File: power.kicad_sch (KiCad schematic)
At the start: 71 parts, among them J7 USB-C_GCT_USB4105-GF-A, J8 Molex_Nano-Fit_1x2_SMD_105430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, Q3 2N7002_SOT-23-3, U13 TPS564247DRLR, U6 TPS564247DRLR, U7 TPS564247DRLR, U8 TPS564247DRLR, U9 TPS564247DRLR

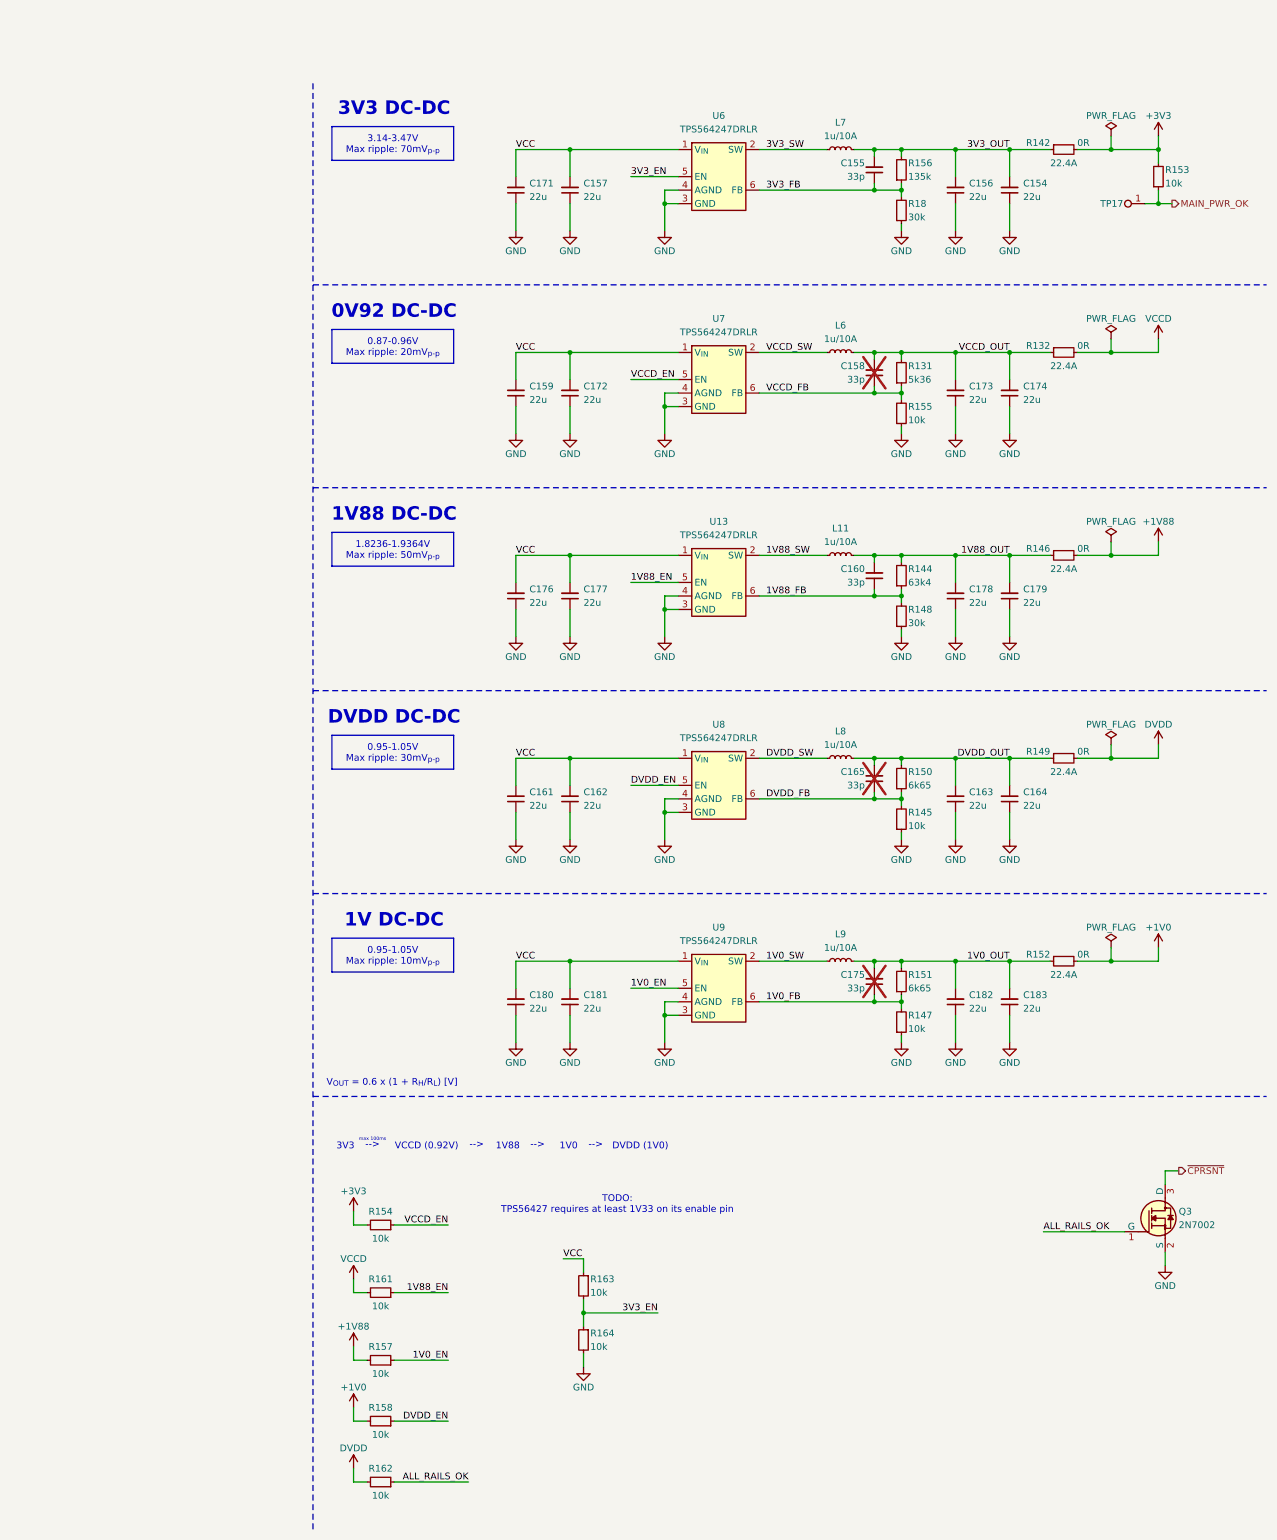
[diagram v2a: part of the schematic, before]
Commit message: [#85196] Draft DC-DC converters with new IC
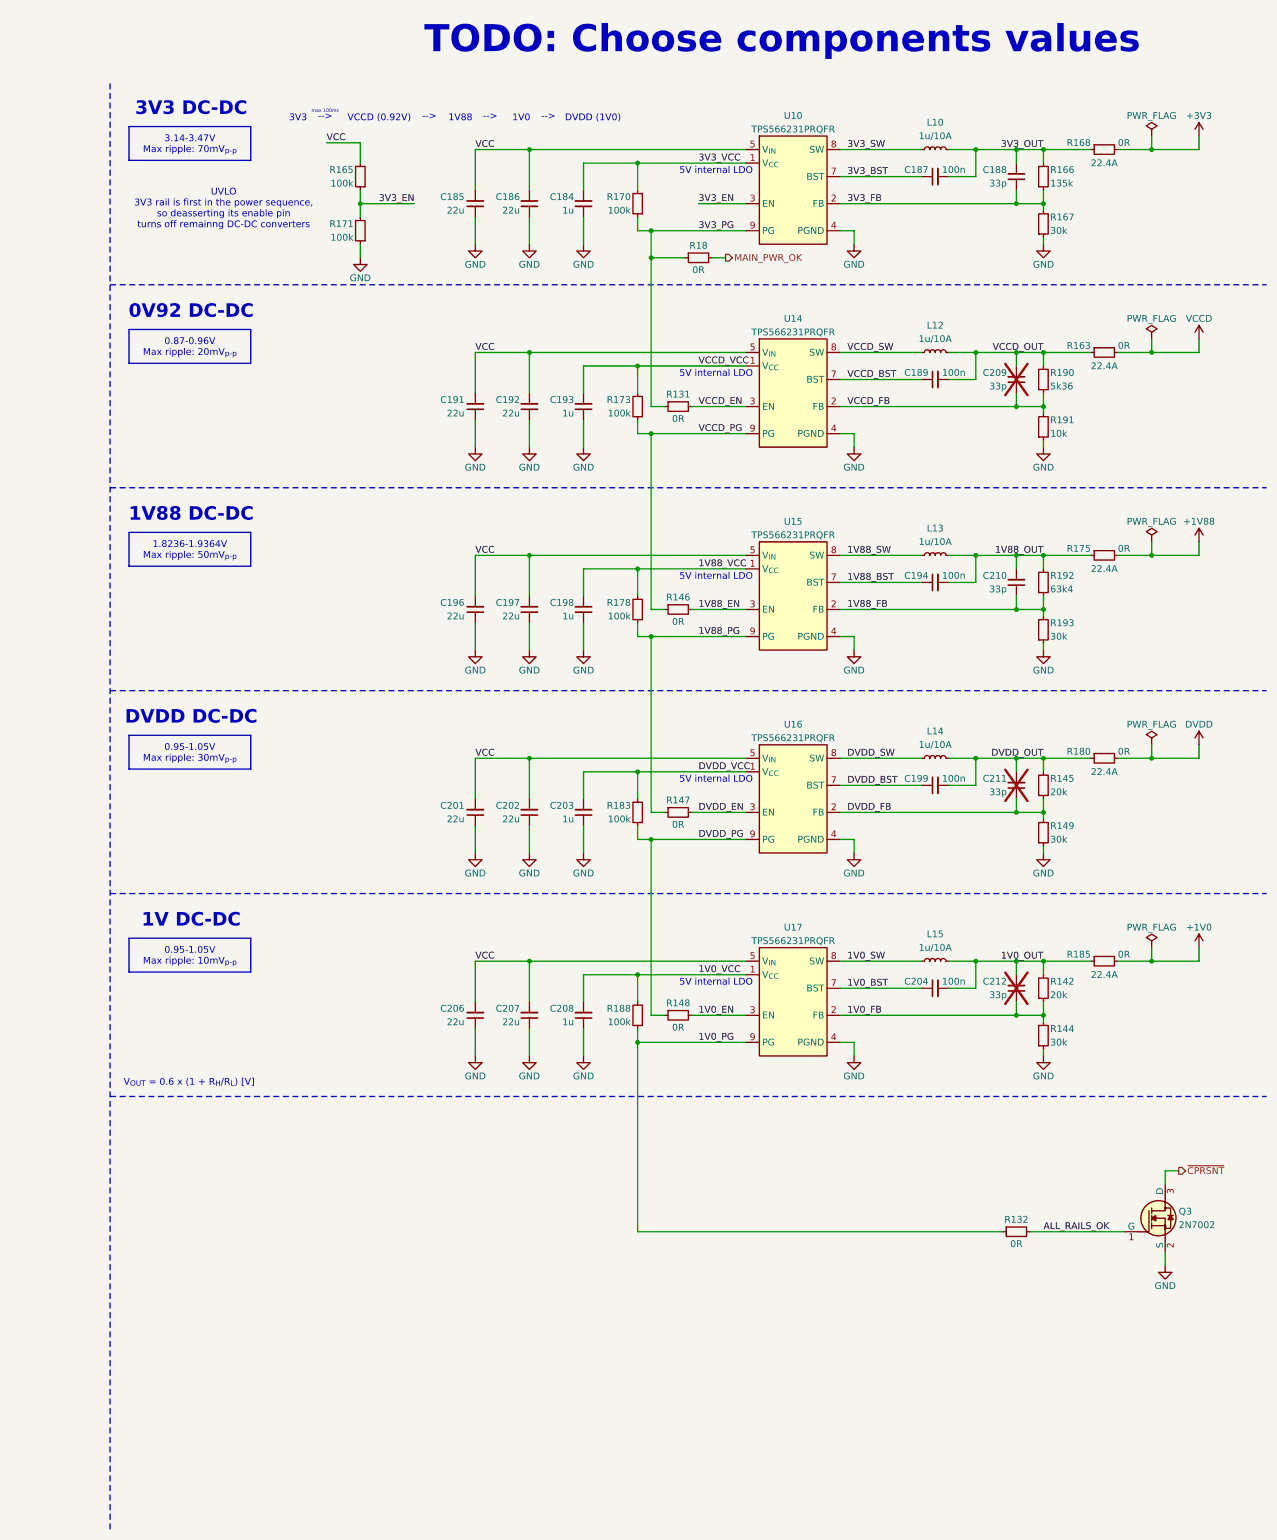
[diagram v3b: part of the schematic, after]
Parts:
- removed C154, C156, C157, C159, C161, C162, C163, C164, C171, C172, C173, C174, C176, C177, C178, C179, C180, C181, C182, C183: C_22u_16V_0603, antmicro-footprints:C_0603_1608Metric_EIA, symbol antmicroCapacitors0603:C_22u_16V_0603
- removed C155, C158, C160, C165, C175: C_33p_0402, antmicro-footprints:C_0402_1005Metric, symbol antmicroCapacitors0402:C_33p_0402
- removed L11, L6, L7, L8, L9: L_1u_10A_Bourns-SRP4021HMT, antmicro-footprints:L_Bourns-SRP4021HMT, symbol antmicroFixedInductors:L_1u_10A_Bourns-SRP4021HMT
- removed R131: R_5k36_0402, antmicro-footprints:R_0402_1005Metric, symbol antmicroResistors0402:R_5k36_0402
- removed R132, R142, R146, R149, R152: R_0R_22.4A_0603, antmicro-footprints:R_0603_1608Metric, symbol antmicroResistors0603:R_0R_22.4A_0603
- removed R144: R_63k4_0402, antmicro-footprints:R_0402_1005Metric, symbol antmicroResistors0402:R_63k4_0402
- removed R145, R147, R155: R_10k_0.1%_0402, antmicro-footprints:R_0402_1005Metric, symbol antmicroResistors0402:R_10k_0.1%_0402
- removed R148, R18: R_30k_0402, antmicro-footprints:R_0402_1005Metric, symbol antmicroResistors0402:R_30k_0402
- removed R150, R151: R_6k65_0402, antmicro-footprints:R_0402_1005Metric, symbol antmicroResistors0402:R_6k65_0402
- removed R153, R154, R157, R158, R161, R162, R163, R164: R_10k_0402, antmicro-footprints:R_0402_1005Metric, symbol antmicroResistors0402:R_10k_0402
- removed R156: R_135k_0402, antmicro-footprints:R_0402_1005Metric, symbol antmicroResistors0402:R_135k_0402
- removed TP17: TP_0.75mm_SMD, antmicro-footprints:TP_SMD_0.75mm, symbol antmicroTestPoints:TP_0.75mm_SMD
- removed U13, U6, U7, U8, U9: TPS564247DRLR, antmicro-footprints:SOT-563, symbol antmicroDCDCConverters:TPS564247DRLR
- added C184, C193, C198, C203, C208: C_1u_25V_0402, antmicro-footprints:C_0402_1005Metric, symbol antmicroCapacitors0402:C_1u_25V_0402
- added C185, C186, C191, C192, C196, C197, C201, C202, C206, C207: C_22u_16V_0603, antmicro-footprints:C_0603_1608Metric_EIA, symbol antmicroCapacitors0603:C_22u_16V_0603
- added C187, C189, C194, C199, C204: C_100n_0402, antmicro-footprints:C_0402_1005Metric, symbol antmicroCapacitors0402:C_100n_0402
- added C188, C209, C210, C211, C212: C_33p_0402, antmicro-footprints:C_0402_1005Metric, symbol antmicroCapacitors0402:C_33p_0402
- added L10, L12, L13, L14, L15: L_1u_10A_Bourns-SRP4021HMT, antmicro-footprints:L_Bourns-SRP4021HMT, symbol antmicroFixedInductors:L_1u_10A_Bourns-SRP4021HMT
- added R131, R132, R146, R147, R148, R18: R_0R_0402, antmicro-footprints:R_0402_1005Metric, symbol antmicroResistors0402:R_0R_0402
- added R142, R145: R_20k_0402, antmicro-footprints:R_0402_1005Metric, symbol antmicroResistors0402:R_20k_0402
- added R144, R149, R167, R193: R_30k_0402, antmicro-footprints:R_0402_1005Metric, symbol antmicroResistors0402:R_30k_0402
- added R163, R168, R175, R180, R185: R_0R_22.4A_0603, antmicro-footprints:R_0603_1608Metric, symbol antmicroResistors0603:R_0R_22.4A_0603
- added R165, R170, R171, R173, R178, R183, R188: R_100k_0402, antmicro-footprints:R_0402_1005Metric, symbol antmicroResistors0402:R_100k_0402
- added R166: R_135k_0402, antmicro-footprints:R_0402_1005Metric, symbol antmicroResistors0402:R_135k_0402
- added R190: R_5k36_0402, antmicro-footprints:R_0402_1005Metric, symbol antmicroResistors0402:R_5k36_0402
- added R191: R_10k_0.1%_0402, antmicro-footprints:R_0402_1005Metric, symbol antmicroResistors0402:R_10k_0.1%_0402
- added R192: R_63k4_0402, antmicro-footprints:R_0402_1005Metric, symbol antmicroResistors0402:R_63k4_0402
- added U10, U14, U15, U16, U17: TPS566231P, antmicro-footprints:VQFN-HR-9_2x1.5mm, symbol antmicroDCDCConverters:TPS566231P
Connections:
- net +1V0: now also R185.2
- net +1V88: now also R175.2
- net +3V3: now also R168.2
- net 1V0_EN: now also R148.2, U17.3 (EN)
- net 1V0_FB: now also C212.1, R142.1, R144.2, U17.2 (FB)
- net 1V0_OUT: now also C204.2, C212.2, L15.2, R142.2, R185.1
- net 1V0_SW: now also L15.1, U17.8 (SW)
- net 1V88_EN: now also R146.2, U15.3 (EN)
- net 1V88_FB: now also C210.1, R192.1, R193.2, U15.2 (FB)
- net 1V88_OUT: now also C194.2, C210.2, L13.2, R175.1, R192.2
- net 1V88_SW: now also L13.1, U15.8 (SW)
- net 3V3_EN: now also R165.1, R171.2, U10.3 (EN)
- net 3V3_FB: now also C188.1, R166.1, R167.2, U10.2 (FB)
- net 3V3_OUT: now also C187.2, C188.2, L10.2, R166.2, R168.1
- net 3V3_SW: now also L10.1, U10.8 (SW)
- net ALL_RAILS_OK: now also R132.2
- net DVDD: now also R180.2
- net DVDD_EN: now also R147.2, U16.3 (EN)
- net DVDD_FB: now also C211.1, R145.1, R149.2, U16.2 (FB)
- net DVDD_OUT: now also C199.2, C211.2, L14.2, R145.2, R180.1
- net DVDD_SW: now also L14.1, U16.8 (SW)
- net GND: now also C184.1, C185.1, C186.1, C191.1, C192.1, C193.1, C196.1, C197.1, C198.1, C201.1, C202.1, C203.1, C206.1, C207.1, C208.1, R144.1, R149.1, R167.1, R171.1, R191.1, R193.1, U10.4 (PGND), U14.4 (PGND), U15.4 (PGND), U16.4 (PGND), U17.4 (PGND)
- net MAIN_PWR_OK: now also R18.2
- net VCC: now also C185.2, C186.2, C191.2, C192.2, C196.2, C197.2, C201.2, C202.2, C206.2, C207.2, R165.2, U10.5 (V_{IN}), U10.6 (V_{IN}), U14.5 (V_{IN}), U14.6 (V_{IN}), U15.5 (V_{IN}), U15.6 (V_{IN}), U16.5 (V_{IN}), U16.6 (V_{IN}), U17.5 (V_{IN}), U17.6 (V_{IN})
- net VCCD: now also R163.2
- net VCCD_EN: now also R131.2, U14.3 (EN)
- net VCCD_FB: now also C209.1, R190.1, R191.2, U14.2 (FB)
- net VCCD_OUT: now also C189.2, C209.2, L12.2, R163.1, R190.2
- net VCCD_SW: now also L12.1, U14.8 (SW)
- new net 1V0_BST: C204.1, U17.7 (BST)
- new net 1V0_PG: R132.1, R188.1, U17.9 (PG)
- new net 1V0_VCC: C208.2, R188.2, U17.1 (V_{CC})
- new net 1V88_BST: C194.1, U15.7 (BST)
- new net 1V88_PG: R147.1, R178.1, U15.9 (PG)
- new net 1V88_VCC: C198.2, R178.2, U15.1 (V_{CC})
- new net 3V3_BST: C187.1, U10.7 (BST)
- new net 3V3_PG: R131.1, R170.1, R18.1, U10.9 (PG)
- new net 3V3_VCC: C184.2, R170.2, U10.1 (V_{CC})
- new net DVDD_BST: C199.1, U16.7 (BST)
- new net DVDD_PG: R148.1, R183.1, U16.9 (PG)
- new net DVDD_VCC: C203.2, R183.2, U16.1 (V_{CC})
- new net VCCD_BST: C189.1, U14.7 (BST)
- new net VCCD_PG: R146.1, R173.1, U14.9 (PG)
- new net VCCD_VCC: C193.2, R173.2, U14.1 (V_{CC})
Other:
- note added: "5V internal LDO"
- note added: "TODO: Choose components values"
- note added: "UVLO 3V3 rail is first in the power sequence, so deasserting its enable pin turns off remainng DC-DC converters"
- note removed: "TODO: TPS56427 requires at least 1V33 on its enable pin"

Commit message: [#85196] Finish design of all power rails DC-DC converters
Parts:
- removed L10: L_1u_10A_Bourns-SRP4021HMT, antmicro-footprints:L_Bourns-SRP4021HMT, symbol antmicroFixedInductors:L_1u_10A_Bourns-SRP4021HMT
- removed R165: R_100k_0402, antmicro-footprints:R_0402_1005Metric, symbol antmicroResistors0402:R_100k_0402
- removed R190: R_5k36_0402, antmicro-footprints:R_0402_1005Metric, symbol antmicroResistors0402:R_5k36_0402
- removed R191: R_10k_0.1%_0402, antmicro-footprints:R_0402_1005Metric, symbol antmicroResistors0402:R_10k_0.1%_0402
- added C154, C155, C156, C157, C158, C159, C160, C161, C162, C163: C_22u_16V_0603, antmicro-footprints:C_0603_1608Metric_EIA, symbol antmicroCapacitors0603:C_22u_16V_0603
- added C164, C165, C171, C172, C173, C174, C175, C176, C177, C178: C_100n_0402, antmicro-footprints:C_0402_1005Metric, symbol antmicroCapacitors0402:C_100n_0402
- added L7: L_2u2_8A_Coilcraft-XFL4020, antmicro-footprints:L_Coilcraft-XFL4020, symbol antmicroFixedInductors:L_2u2_8A_Coilcraft-XFL4020
- added R150: R_255k_0402, antmicro-footprints:R_0402_1005Metric, symbol antmicroResistors0402:R_255k_0402
- added R151: R_16k_0402, antmicro-footprints:R_0402_1005Metric, symbol antmicroResistors0402:R_16k_0402
- added R152: R_30k_0402, antmicro-footprints:R_0402_1005Metric, symbol antmicroResistors0402:R_30k_0402
- C210: now not fitted
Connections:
- net 1V0_OUT: now also C162.2, C163.2, C178.2
- net 1V88_OUT: now also C158.2, C159.2, C174.2
- net 3V3_EN: now also R150.1
- net 3V3_OUT: now also C154.2, C155.2, C172.2, L7.2
- net 3V3_SW: now also L7.1
- net DVDD_OUT: now also C160.2, C161.2, C177.2
- net GND: now also C154.1, C155.1, C156.1, C157.1, C158.1, C159.1, C160.1, C161.1, C162.1, C163.1, C164.1, C165.1, C171.1, C172.1, C173.1, C174.1, C175.1, C176.1, C177.1, C178.1, R152.1
- net VCC: now also C165.2, C171.2, C173.2, C175.2, C176.2, R150.2
- net VCCD_FB: now also R151.1, R152.2
- net VCCD_OUT: now also C156.2, C157.2, C164.2, R151.2
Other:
- note removed: "TODO: Choose components values"
- moved on the sheet: C166, C184, C185, C186, C187, C188, C189, C191, C192, C193, C194, C196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

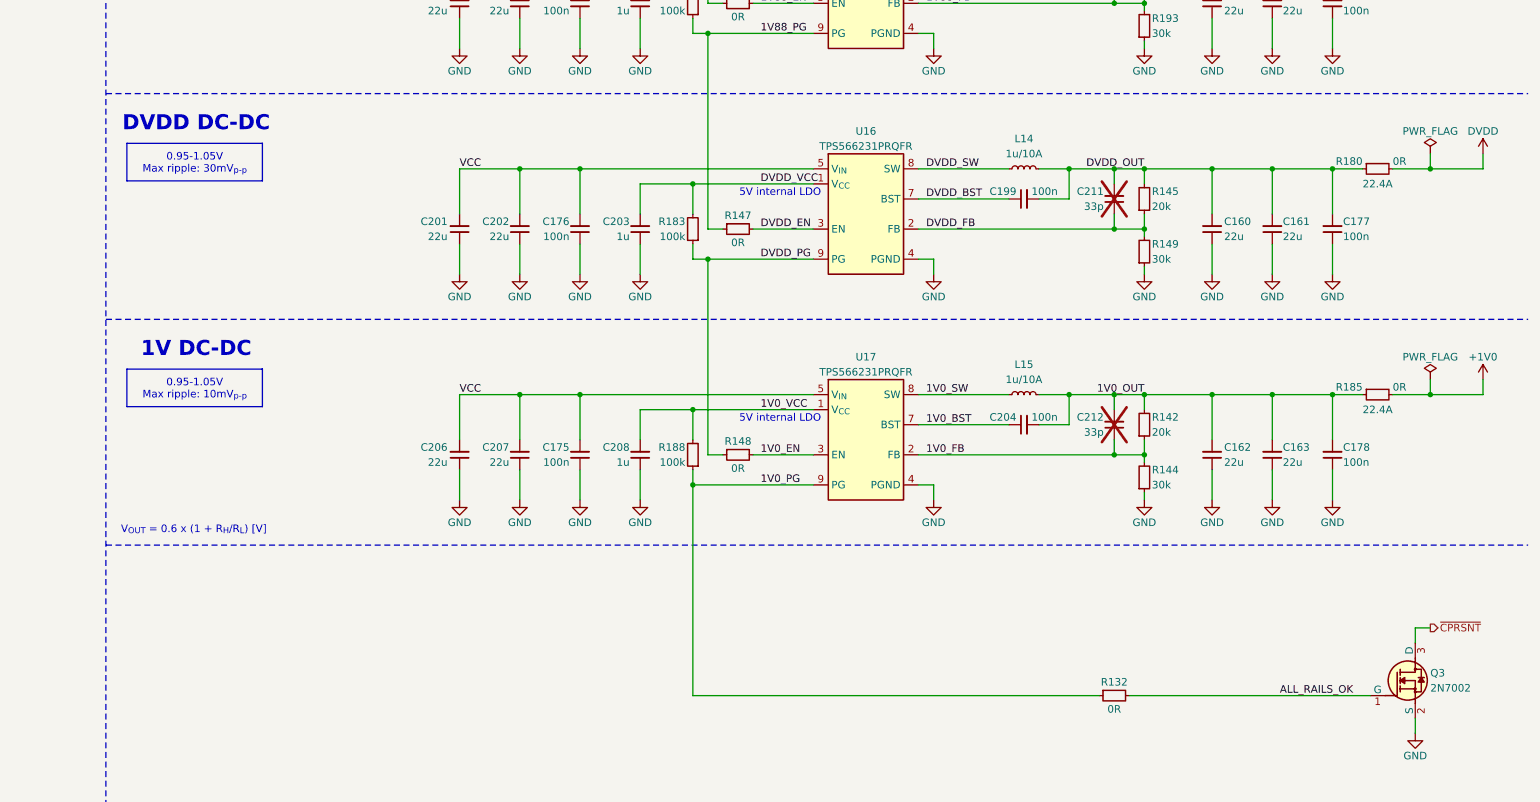
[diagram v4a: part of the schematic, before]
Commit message: [#85196] Fix 1V0 and DVDD sequencing
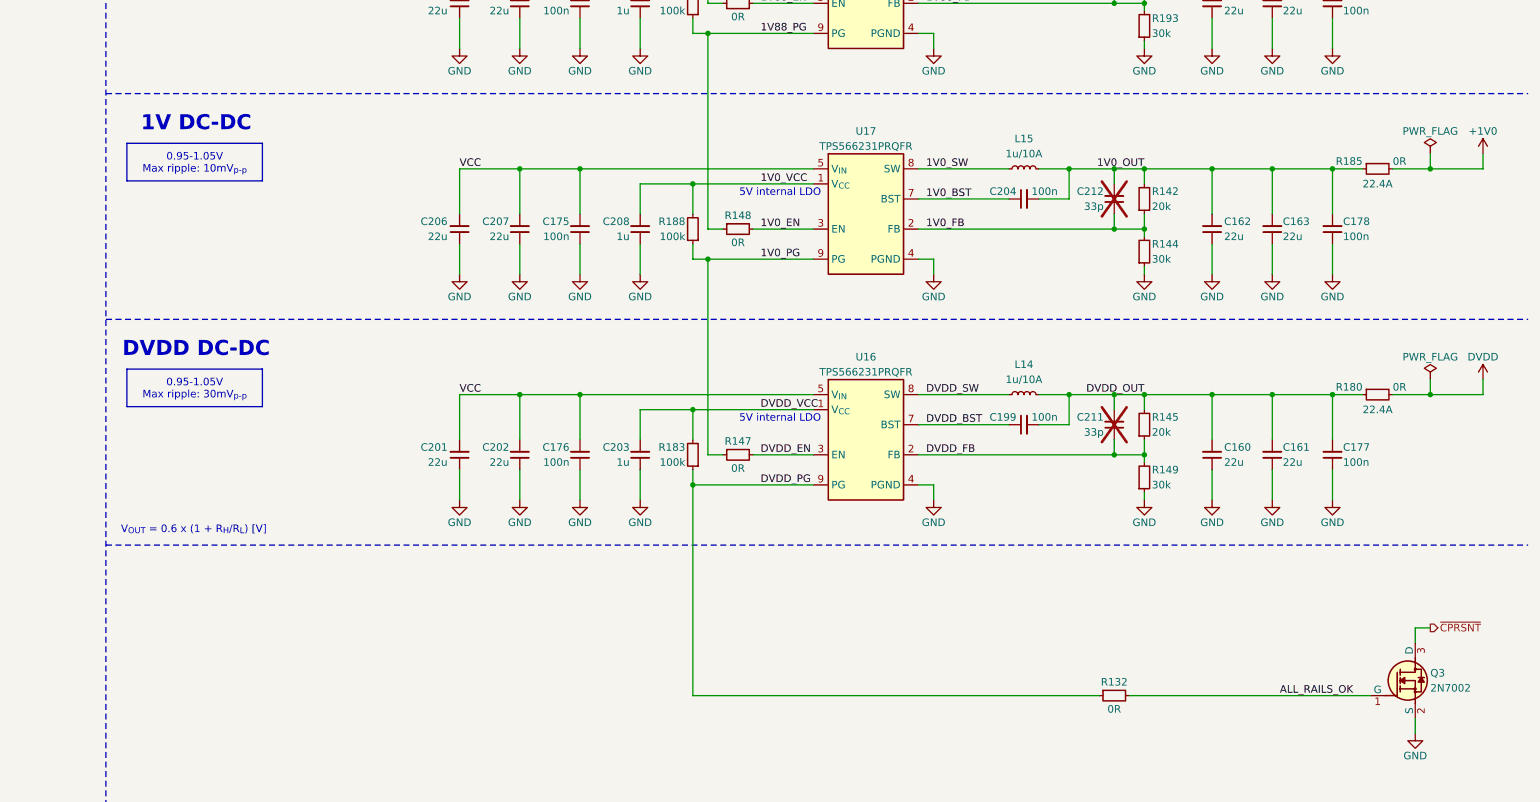
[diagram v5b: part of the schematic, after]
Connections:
- net 1V0_PG: now also R147.1; no longer R132.1
- net 1V88_PG: now also R148.1; no longer R147.1
- net DVDD_PG: now also R132.1; no longer R148.1
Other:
- moved on the sheet: C160, C161, C162, C163, C175, C176, C177, C178, C199, C201, C202, C203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
